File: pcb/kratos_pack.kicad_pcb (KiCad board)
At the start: 4 copper layers, 44.2 x 20.2 mm, 121 parts, among them J1 USB_C_Receptacle_USB2.0, J2 PROG_CONN, J3 DBG_UART, J4 BAT_MID+NTC, J5 BAT_7.4V, J6 BAT_0V, J7 OUT+, J8 OUT-, Q1 AON7403, Q2 AON7414, Q3 AON7414, Q4 UT6MA2TCR, Q5 UT6MA2TCR, Q6 UT6MA2TCR, Q7 DMN2450UFD, SW1 WAKEUP, SW2 BOOT, SW3 RST_BTN, U1 USBLC6-2SC6, U10 24LC32, U11 MIC94300, U12 74LVC2G14, U13 MIC94300, U2 CP2102N-Axx-xQFN20, U3 STM32G071Gx, U4 KTD2026BEWE, U5 BQ25887, U6 BD48xxFVE, U7 INA199, U8 LTC4231, U9 LDK715M33R

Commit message: Schema & PCB: Fix USB detection by MCU and USB converter, hide GND labels
USB detection circuit is now connected only to MCU.
Converter from USB to UART (CP2102) is directly connected to VBUS.
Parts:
- R14: value 10k -> DNP
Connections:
- U2 pad 8: /USB_DET -> VBUS
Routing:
- net /USB_DET: track 31.8 -> 23.0 mm, vias 4 -> 3
- net VBUS: track 52.3 -> 52.8 mm
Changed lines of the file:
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@@
       (effects (font (size 1 1) (thickness 0.15)))
     )
-    (fp_text value "10k" (at 0 1.43) (layer "F.Fab")
+    (fp_text value "DNP" (at 0 1.43) (layer "F.Fab")
       (effects (font (size 1 1) (thickness 0.15)))
     )
@@
       (net 76 "VBUS") (pinfunction "VREGIN") (pintype "power_in"))
     (pad "8" smd rect locked (at -0.25 -1.55 270) (size 0.9 0.3) (layers "B.Cu" "B.Paste" "B.Mask")
-      (net 22 "/USB_DET") (pinfunction "VBUS") (pintype "input"))
+      (net 76 "VBUS") (pinfunction "VBUS") (pintype "input"))
     (pad "9" smd rect locked (at 0.25 -1.55 270) (size 0.9 0.3) (layers "B.Cu" "B.Paste" "B.Mask")
       (net 54 "Net-(R7-Pad2)") (pinfunction "~{RST}") (pintype "input"))
@@
   (segment (start 136.93 105.475) (end 135.85 105.475) (width 0.127) (layer "B.Cu") (net 21))
   (via (at 133.6 94.7) (size 0.5) (drill 0.2) (layers "F.Cu" "B.Cu") (net 22))
-  (via (at 135.66 91.06) (size 0.5) (drill 0.2) (layers "F.Cu" "B.Cu") (net 22))
   (via (at 146.6 93.5) (size 0.5) (drill 0.2) (layers "F.Cu" "B.Cu") (net 22))
   (via (at 141.88 92.07) (size 0.5) (drill 0.2) (layers "F.Cu" "B.Cu") (net 22))
-  (segment (start 133.6 93.85) (end 133.6 94.7) (width 0.127) (layer "In2.Cu") (net 22))
   (segment (start 133.6 95.525) (end 133.6 94.7) (width 0.127) (layer "In2.Cu") (net 22))
-  (segment (start 134.915 91.075) (end 134 91.99) (width 0.127) (layer "In2.Cu") (net 22))
   (segment (start 143.735 93.46) (end 144.61 93.46) (width 0.127) (layer "In2.Cu") (net 22))
   (segment (start 144.791499 93.278501) (end 146.378501 93.278501) (width 0.127) (layer "In2.Cu") (net 22))
-  (segment (start 134 93.45) (end 133.6 93.85) (width 0.127) (layer "In2.Cu") (net 22))
   (segment (start 144.61 93.46) (end 144.791499 93.278501) (width 0.127) (layer "In2.Cu") (net 22))
   (segment (start 137.275 96.675) (end 134.75 96.675) (width 0.127) (layer "In2.Cu") (net 22))
   (segment (start 146.378501 93.278501) (end 146.6 93.5) (width 0.127) (layer "In2.Cu") (net 22))
   (segment (start 142.4625 92.9625) (end 143.2375 92.9625) (width 0.127) (layer "In2.Cu") (net 22))
-  (segment (start 134.915 91.075) (end 134.93 91.06) (width 0.127) (layer "In2.Cu") (net 22))
   (segment (start 141.88 92.07) (end 141.88 92.38) (width 0.127) (layer "In2.Cu") (net 22))
   (segment (start 134.75 96.675) (end 133.6 95.525) (width 0.127) (layer "In2.Cu") (net 22))
@@
   (segment (start 141.88 92.38) (end 142.4625 92.9625) (width 0.127) (layer "In2.Cu") (net 22))
   (segment (start 141.88 92.07) (end 137.275 96.675) (width 0.127) (layer "In2.Cu") (net 22))
-  (segment (start 134.93 91.06) (end 135.66 91.06) (width 0.127) (layer "In2.Cu") (net 22))
-  (segment (start 134 91.99) (end 134 93.45) (width 0.127) (layer "In2.Cu") (net 22))
   (segment (start 133.6 94.7) (end 133.6 94.425) (width 0.127) (layer "B.Cu") (net 22))
   (segment (start 141.875 92.825) (end 141.875 94.175) (width 0.25) (layer "B.Cu") (net 22))
@@
   (segment (start 141.88 92.07) (end 141.875 92.075) (width 0.127) (layer "B.Cu") (net 22))
   (segment (start 147.375 94.2) (end 146.973 94.2) (width 0.127) (layer "B.Cu") (net 22))
-  (segment (start 135.66 91.06) (end 136.01 90.71) (width 0.127) (layer "B.Cu") (net 22))
-  (segment (start 137.25 90.71) (end 137.64 90.32) (width 0.127) (layer "B.Cu") (net 22))
-  (segment (start 138.445 90.32) (end 138.61 90.485) (width 0.127) (layer "B.Cu") (net 22))
-  (segment (start 137.64 90.32) (end 138.445 90.32) (width 0.127) (layer "B.Cu") (net 22))
   (segment (start 141.875 92.075) (end 141.875 92.825) (width 0.127) (layer "B.Cu") (net 22))
   (segment (start 132.475 93.05) (end 132.85 93.425) (width 0.127) (layer "B.Cu") (net 22))
   (segment (start 146.973 94.2) (end 146.6 93.827) (width 0.127) (layer "B.Cu") (net 22))
-  (segment (start 138.61 90.485) (end 138.61 91.08) (width 0.127) (layer "B.Cu") (net 22))
-  (segment (start 136.01 90.71) (end 137.25 90.71) (width 0.127) (layer "B.Cu") (net 22))
   (segment (start 146.6 93.827) (end 146.6 93.5) (width 0.127) (layer "B.Cu") (net 22))
   (segment (start 132.85 93.425) (end 132.85 94.275) (width 0.127) (layer "B.Cu") (net 22))
@@
   (segment (start 142 91.05) (end 141.875 91.175) (width 0.127) (layer "B.Cu") (net 76))
   (segment (start 138.1 91.03) (end 136.32 91.03) (width 0.127) (layer "B.Cu") (net 76))
-  (segment (start 133.425 93.175) (end 133.425 92.15) (width 0.127) (layer "B.Cu") (net 76))
-  (segment (start 133.875 91.7) (end 134.2375 91.7) (width 0.127) (layer "B.Cu") (net 76))
   (segment (start 138.375 95.175) (end 138.15 94.95) (width 0.127) (layer "B.Cu") (net 76))
+  (segment (start 138.11 91.08) (end 138.61 91.08) (width 0.127) (layer "B.Cu") (net 76))
   (segment (start 142.65 91.05) (end 142 91.05) (width 0.127) (layer "B.Cu") (net 76))
   (segment (start 133.1 99.05) (end 133.6 98.55) (width 0.25) (layer "B.Cu") (net 76))
-  (segment (start 134.97 91.7) (end 135.11 91.56) (width 0.127) (layer "B.Cu") (net 76))
-  (segment (start 133.425 92.15) (end 133.875 91.7) (width 0.127) (layer "B.Cu") (net 76))
   (segment (start 136.32 91.03) (end 135.79 91.56) (width 0.127) (layer "B.Cu") (net 76))
+  (segment (start 134.5 91.56) (end 134.36 91.7) (width 0.127) (layer "B.Cu") (net 76))
+  (segment (start 133.425 92.15) (end 133.425 93.175) (width 0.127) (layer "B.Cu") (net 76))
+  (segment (start 133.875 91.7) (end 133.425 92.15) (width 0.127) (layer "B.Cu") (net 76))
   (segment (start 138.375 95.7) (end 138.375 95.175) (width 0.127) (layer "B.Cu") (net 76))
   (segment (start 135.79 91.56) (end 135.11 91.56) (width 0.127) (layer "B.Cu") (net 76))
-  (segment (start 134.2375 91.7) (end 134.97 91.7) (width 0.127) (layer "B.Cu") (net 76))
+  (segment (start 135.11 91.56) (end 134.5 91.56) (width 0.127) (layer "B.Cu") (net 76))
+  (segment (start 134.36 91.7) (end 133.875 91.7) (width 0.127) (layer "B.Cu") (net 76))
   (segment (start 134.175 98.55) (end 134.375 98.75) (width 0.127) (layer "F.Cu") (net 77))
   (segment (start 132.375 99.05) (end 132.875 98.55) (width 0.127) (layer "F.Cu") (net 77))

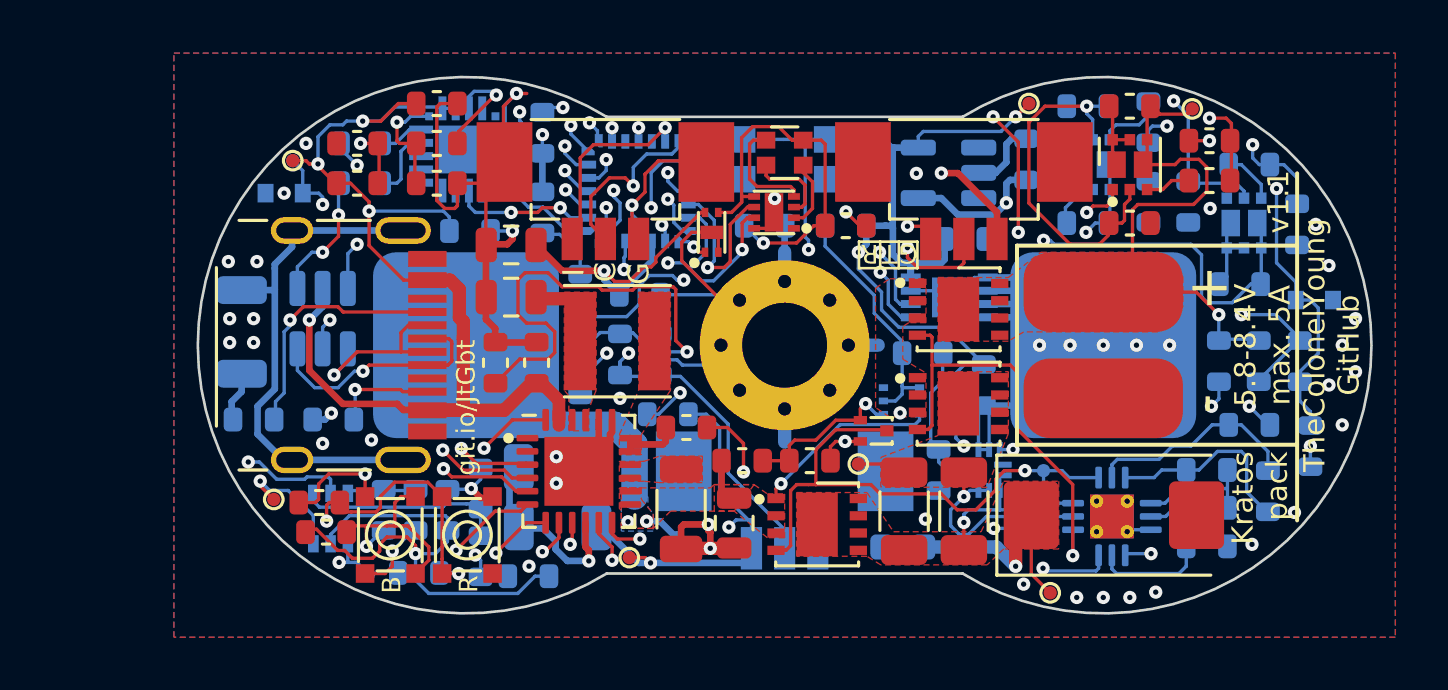
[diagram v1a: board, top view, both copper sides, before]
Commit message: PCB: Fix footprint of signalization LED
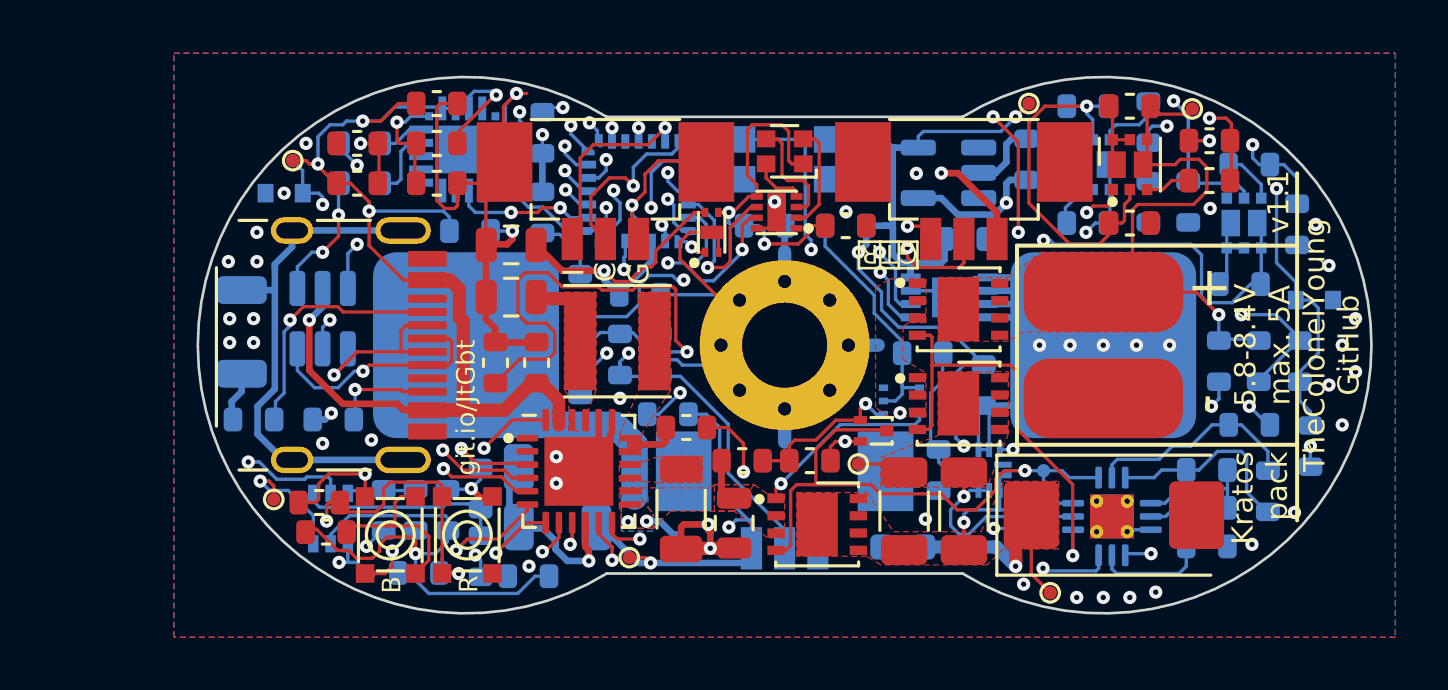
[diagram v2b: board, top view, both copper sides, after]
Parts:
- D2: footprint Resistor_SMD:R_Array_Convex_2x0606 -> TCY_smd_leds:WL-SFCD - RGB606
- moved U4 0.10 mm to (150.7, 95.0)
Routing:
- net Net-(D2-Pad1): track 4.09 -> 2.07 mm
- net /LED_PWR: track 14.3 -> 12.8 mm, vias 1 -> 2
- net Net-(D2-Pad3): track 2.62 -> 4.13 mm
- net Net-(D2-Pad2): track 3.18 -> 4.33 mm
- net GND: track 169.5 -> 168.7 mm, vias 54 -> 55

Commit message: Schema & PCB: connect LTC4231 Shutdown pin to MCU GPIO
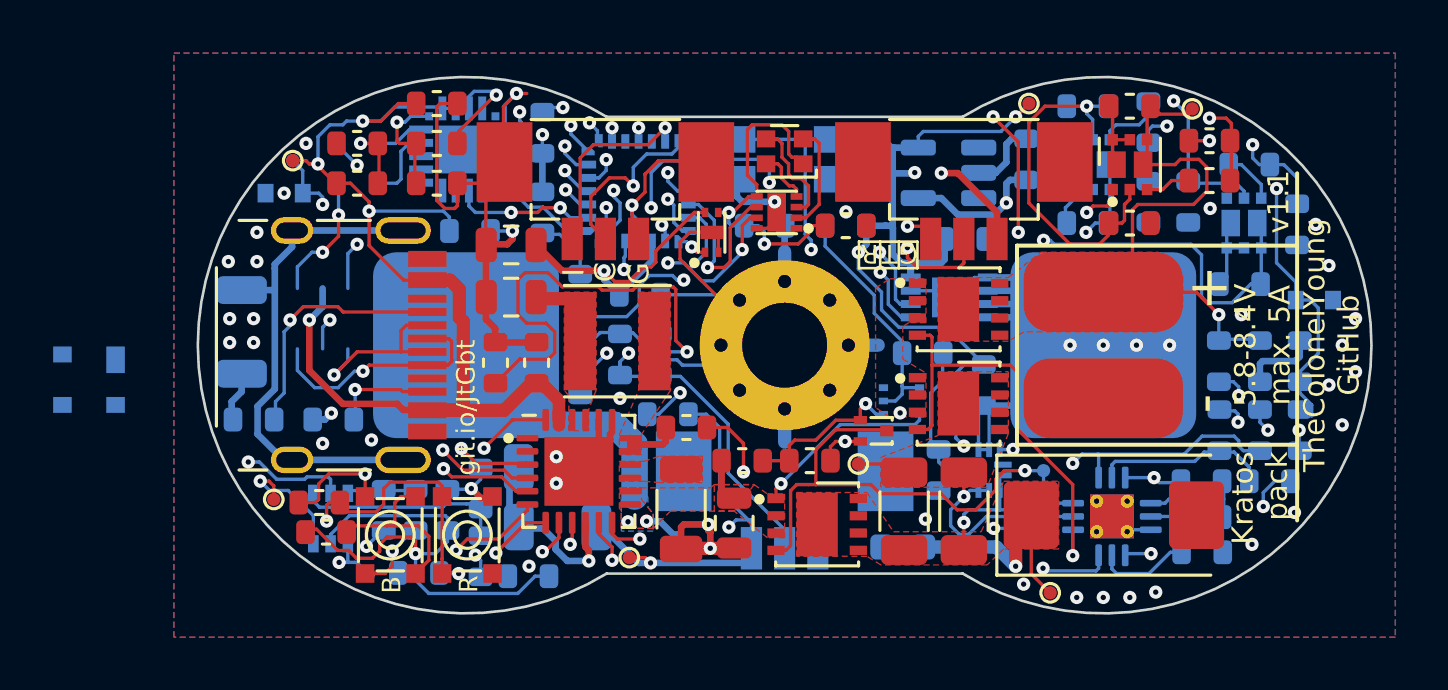
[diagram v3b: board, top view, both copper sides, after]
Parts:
- removed R11: 22R, TCY_passives:R_0603_1608Metric
- removed U1: USBLC6-2SC6, Package_TO_SOT_SMD:SOT-23-6
- added D5: SP0503BAHT, Package_TO_SOT_SMD:SOT-143, B.Cu at (124.8, 101.3)
- R10: value 22R -> 4.02k
- moved R10 35.1 mm to (168.9, 103.2), turned to 90 degrees
- moved R25 1.14 mm to (167.4, 103.2), turned to -90 degrees
- moved R41 0.72 mm to (170.4, 103.2)
- moved R27 0.47 mm to (166.7, 105.1)
- moved R30 0.40 mm to (166.7, 106.5)
- moved R26 0.38 mm to (169.3, 105.1), turned to 0 degrees
- moved C20 0.29 mm to (166.7, 107.8)
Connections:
- J1 pad A6: Net-(J1-PadA6) -> /D+
- J1 pad A7: Net-(J1-PadA7) -> /D-
- J1 pad B6: Net-(J1-PadA6) -> /D+
- J1 pad B7: Net-(J1-PadA7) -> /D-
- R10 pad 1: Net-(R10-Pad1) -> /SHDN
- R10 pad 2: /D+ -> +3V3
- U2 pad 8: VBUS -> /USB_DET
- U3 pad 22: unconnected-(U3-Pad22) -> /SHDN
- U8 pad 1: /UVLO -> /SHDN
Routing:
- net /SHDN: track 0.00 -> 46.4 mm, vias 0 -> 4
- net +3V3: track 89.6 -> 116.6 mm, vias 4 -> 6
- net Net-(J1-PadA6): track 9.01 -> 0.00 mm, vias 1 -> 0
- net /D+: track 2.68 -> 11.7 mm, vias 0 -> 1
- net Net-(R26-Pad2): track 7.38 -> 14.8 mm, vias 0 -> 2
- net Net-(J1-PadA7): track 6.95 -> 0.00 mm, vias 1 -> 0
- net /D-: track 1.65 -> 8.60 mm, vias 0 -> 1
- net Net-(R11-Pad1): track 5.81 -> 0.00 mm, vias 2 -> 0
- net (no net): track 0.00 -> 5.81 mm, vias 0 -> 2
- net Net-(R10-Pad1): track 4.81 -> 0.00 mm, vias 2 -> 0
- net /UVLO: track 21.1 -> 18.9 mm
- net Net-(R25-Pad2): track 8.07 -> 6.62 mm
- net Net-(R32-Pad2): track 8.48 -> 9.47 mm
- net VCC: track 56.3 -> 55.5 mm
- net Net-(C20-Pad1): track 4.25 -> 3.54 mm
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
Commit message: PCB: fix USB connection, change ESD protection IC
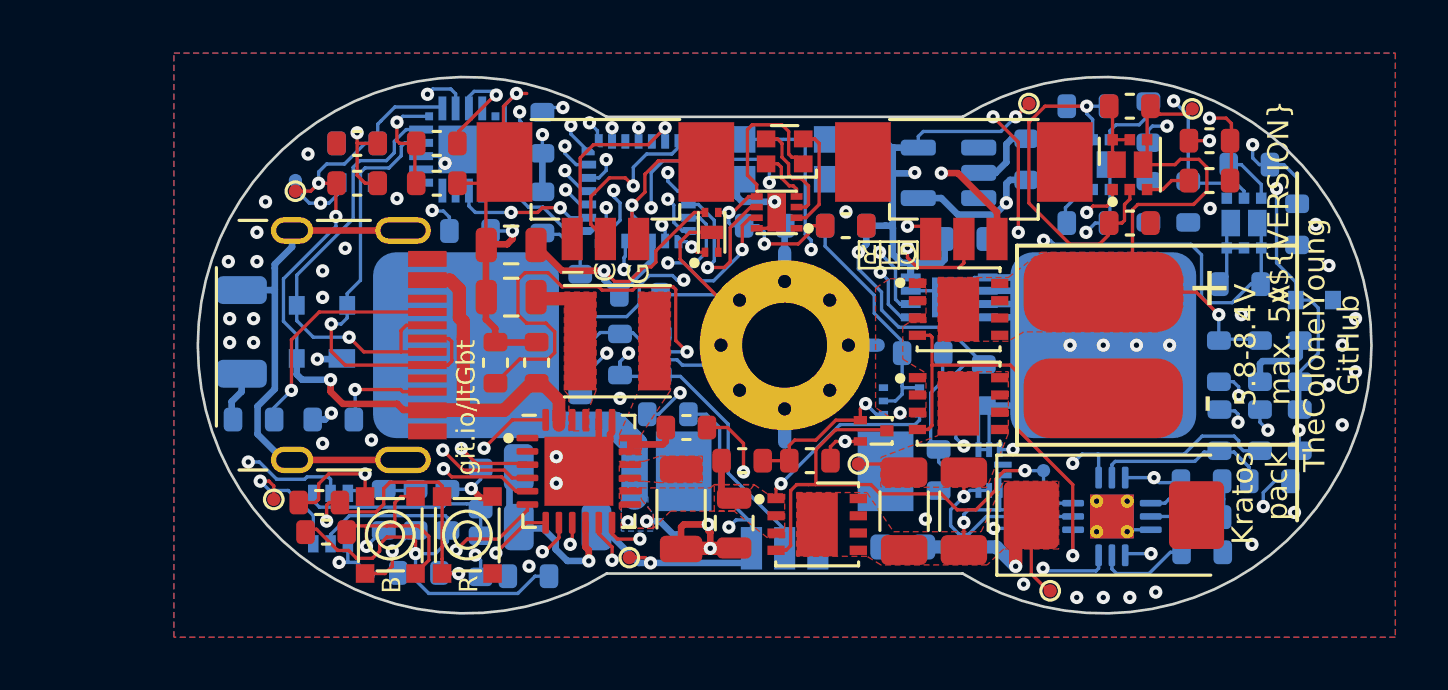
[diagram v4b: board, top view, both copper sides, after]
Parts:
- C6: moved to B.Cu
- moved D5 8.96 mm to (133.6, 99.5), turned to 90 degrees
- moved C6 3.35 mm to (134.9, 92.4), turned to 180 degrees
- moved D1 2.78 mm to (134.9, 93.9), turned to 0 degrees
- moved TP2 1.15 mm to (132.6, 94.2)
- moved TP1 0.76 mm to (132.6, 93.8)
- moved TP6 0.08 mm to (161.0, 109.2)
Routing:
- net /USB_DET: track 23.0 -> 32.5 mm, vias 3 -> 4
- net /D-: track 8.60 -> 17.3 mm
- net GND: track 168.8 -> 162.4 mm, vias 53 -> 58
- net (no net): track 5.81 -> 0.00 mm, vias 2 -> 0
- net /D+: track 11.7 -> 16.9 mm
- net /SHDN: track 46.4 -> 41.6 mm, vias 4 -> 2
- net VBUS: track 52.8 -> 48.8 mm
- net Net-(R14-Pad2): track 10.4 -> 11.6 mm
- net Net-(J1-PadA5): track 9.34 -> 8.82 mm
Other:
- board text added: "v${VERSION}"
- board text removed: "v1.1"

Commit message: Schema & PCB: add jumper selector for 3V3 rail regulator supply (VCC/SNS)
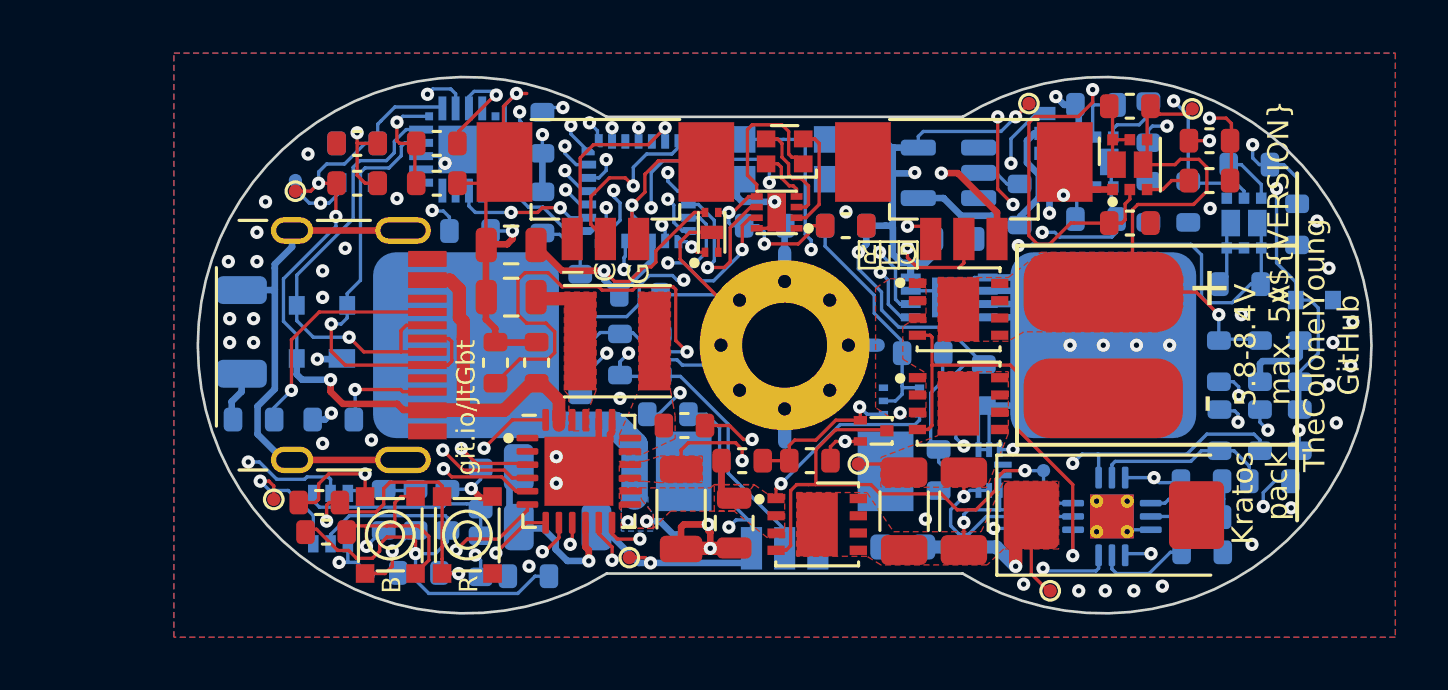
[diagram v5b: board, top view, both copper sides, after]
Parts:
- added JP1: PWR_SEL, TCY_connectors:SolderJumper-3_P0.75mm_Open_Pad0.5x0.8mm, B.Cu at (160.8, 92.0)
- Q7: value DMN2450UFD -> DMN2300UFD-7
- moved C22 1.72 mm to (159.8, 94.7)
- moved C21 0.40 mm to (157.4, 96.0)
- moved R38 0.36 mm to (162.7, 95.2)
- moved R37 0.33 mm to (162.7, 91.0)
- moved Q5 0.16 mm to (162.7, 93.1)
- moved C9 0.11 mm to (147.2, 103.0)
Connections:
- C22 pad 1: VCC -> Net-(C22-Pad1)
- U9 pad 4: VCC -> Net-(C22-Pad1)
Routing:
- net /SNS: track 0.00 -> 24.3 mm, vias 0 -> 2
- net Net-(C22-Pad1): track 0.00 -> 8.70 mm
- net VCC: track 55.5 -> 47.7 mm
- net /CS_EN: track 35.1 -> 29.6 mm
- net GND: track 162.4 -> 166.2 mm, vias 58 -> 59
- net /B1_V: track 40.9 -> 44.5 mm
- net Net-(C9-Pad2): track 2.56 -> 0.00 mm
- net /ME_EN: track 42.2 -> 44.4 mm
- net Net-(C9-Pad1): track 9.19 -> 9.84 mm
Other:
- board text added: "PSEL"
- board text added: "S"
- board text added: "V"
